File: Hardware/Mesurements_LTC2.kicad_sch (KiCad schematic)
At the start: 12 parts, among them Q2 NPN, U2 BQ79614PAPRQ1

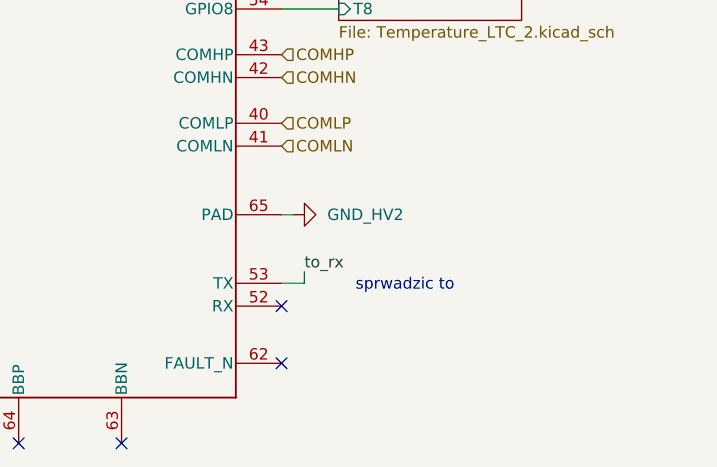
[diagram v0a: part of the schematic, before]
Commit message: Dodano diody TVS na każdej części zasilania, zmieniono bezpieczniki, podzielono bezpieczniki na bezpieczniki do prądów wewnętrznych oraz zewnętrznych,poprawiono małe błedy
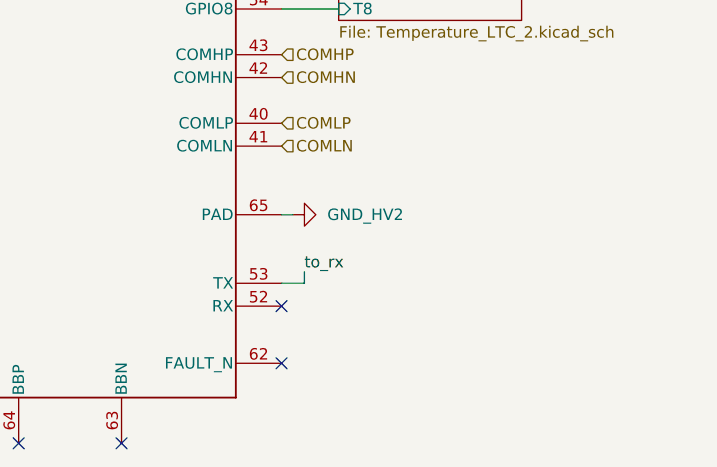
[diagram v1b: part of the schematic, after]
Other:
- note removed: "sprwadzic to"
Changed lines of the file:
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@@
 	(generator_version "9.0")
 	(paper "A4")
-	(text "sprwadzic to\n"
-		(exclude_from_sim no)
-		(at 150.876 131.064 0)
-		(effects
-			(font
-				(size 1.27 1.27)
-			)
-		)
-	)
 	(text "max 370ohm\n"
 		(exclude_from_sim no)

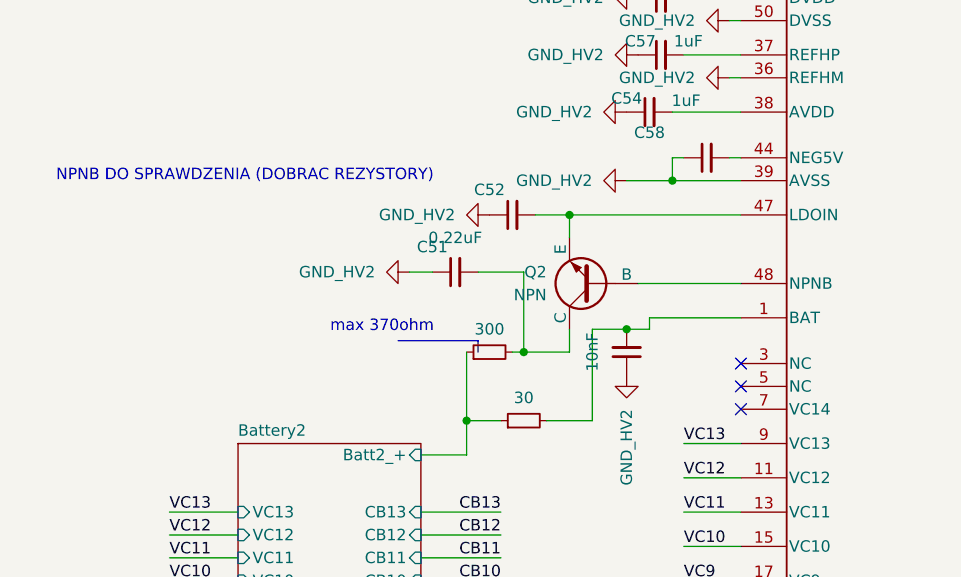
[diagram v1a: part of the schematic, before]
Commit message: dodano pozostale datasheety, zmieniono blad w usb
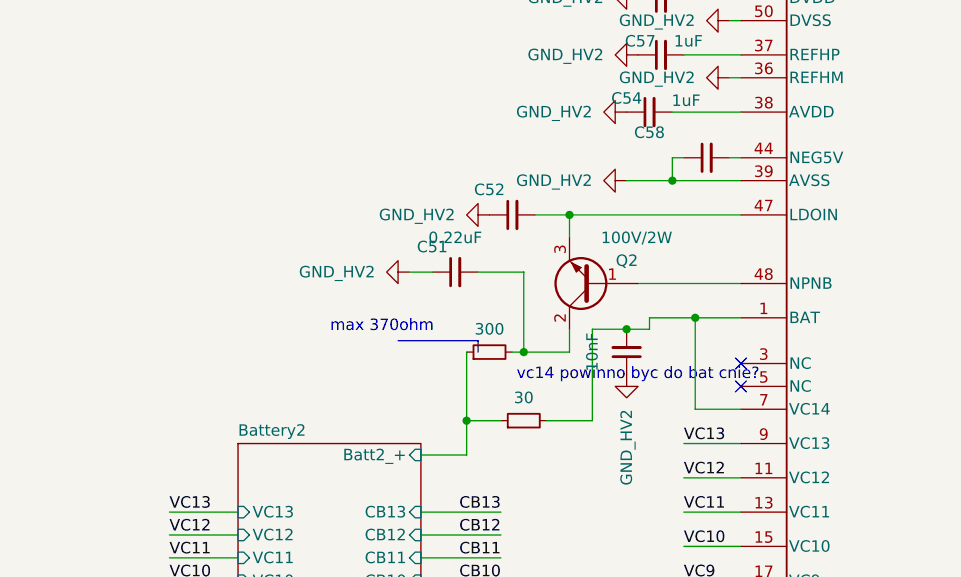
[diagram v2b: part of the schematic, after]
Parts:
- removed Q2: NPN, Package_TO_SOT_SMD:SOT-223-3_TabPin2, symbol Simulation_SPICE:NPN
- added Q2: 100V/2W, Package_TO_SOT_SMD:SOT-223-3_TabPin2, symbol Device:Q_NPN_BCE
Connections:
- net at C53.2, R66.2, U2.1 (BAT): now also U2.7 (VC14)
- net at C52.2, U2.47 (LDOIN): now also Q2.3 (E)
- net at U2.48 (NPNB): now also Q2.1 (B)
- net at C51.2, R64.2: now also Q2.2 (C)
- no-connect marks 10 -> 9
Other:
- note added: "vc14 powinno byc do bat cnie?"
- note removed: "NPNB DO SPRAWDZENIA (DOBRAC REZYSTORY)"
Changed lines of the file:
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@@
 	(generator_version "9.0")
 	(paper "A4")
-	(text "max 370ohm\n"
+	(text "vc14 powinno byc do bat cnie?\n"
 		(exclude_from_sim no)
-		(at 51.562 78.486 0)
+		(at 80.01 83.82 0)
 		(effects
 			(font
@@
 		)
 	)
-	(text "NPNB DO SPRAWDZENIA (DOBRAC REZYSTORY)\n"
+	(text "max 370ohm\n"
 		(exclude_from_sim no)
-		(at 36.322 61.722 0)
+		(at 51.562 78.486 0)
 		(effects
 			(font
@@
 	)
 	(junction
+		(at 86.36 77.47)
+		(diameter 0)
+		(color 0 0 0 0)
+	)
+	(junction
 		(at 60.96 88.9)
 		(diameter 0)
@@
 		(at 137.16 139.7)
 	)
-	(no_connect
-		(at 91.44 87.63)
-	)
 	(wire
 		(pts
@@
 	(wire
 		(pts
-			(xy 81.28 77.47) (xy 91.44 77.47)
+			(xy 81.28 77.47) (xy 86.36 77.47)
 		)
 		(stroke
@@
 	(wire
 		(pts
+			(xy 91.44 87.63) (xy 86.36 87.63)
+		)
+		(stroke
+			(width 0)
+			(type default)
+		)
+	)
+	(wire
+		(pts
 			(xy 67.31 72.39) (xy 62.23 72.39)
 		)
@@
 	(wire
 		(pts
+			(xy 86.36 87.63) (xy 86.36 77.47)
+		)
+		(stroke
+			(width 0)
+			(type default)
+		)
+	)
+	(wire
+		(pts
 			(xy 85.09 48.26) (xy 91.44 48.26)
 		)
@@
 	(wire
 		(pts
+			(xy 86.36 77.47) (xy 91.44 77.47)
+		)
+		(stroke
+			(width 0)
+			(type default)
+		)
+	)
+	(wire
+		(pts
 			(xy 74.93 88.9) (xy 74.93 78.74)
 		)
@@
 	)
 	(symbol
+		(lib_id "Device:Q_NPN_BCE")
+		(at 74.93 73.66 180)
+		(unit 1)
+		(exclude_from_sim no)
+		(in_bom yes)
+		(on_board yes)
+		(dnp no)
+		(property "Reference" "Q2"
+			(at 80.01 71.12 0)
+			(effects
+				(font
+					(size 1.27 1.27)
+				)
+				(justify left)
+			)
+		)
+		(property "Value" "100V/2W"
+			(at 83.82 68.58 0)
+			(effects
+				(font
+					(size 1.27 1.27)
+				)
+				(justify left)
+			)
+		)
+		(property "Footprint" "Package_TO_SOT_SMD:SOT-223-3_TabPin2"
+			(at 69.85 76.2 0)
+			(effects
+				(font
+					(size 1.27 1.27)
+				)
+				(hide yes)
+			)
+		)
+		(property "Datasheet" "https://eu.mouser.com/ProductDetail/Diodes-Incorporated/FZT653TA?qs=rI7uf1IzohQqmHMCtqURKQ%3D%3D"
+			(at 74.93 73.66 0)
+			(effects
+				(font
+					(size 1.27 1.27)
+				)
+				(hide yes)
+			)
+		)
+		(property "Description" "NPN transistor, base/collector/emitter"
+			(at 74.93 73.66 0)
+			(effects
+				(font
+					(size 1.27 1.27)
+				)
+				(hide yes)
+			)
+		)
+		(property "TME Electronic Components Part Number" ""
+			(at 74.93 73.66 0)
+			(effects
+				(font
+					(size 1.27 1.27)
+				)
+				(hide yes)
+			)
+		)
+		(property "TME Electronic Components Price/Stock" ""
+			(at 74.93 73.66 0)
+			(effects
+				(font
+					(size 1.27 1.27)
+				)
+				(hide yes)
+			)
+		)
+		(property "Arrow Part Number" ""
+			(at 74.93 73.66 0)
+			(effects
+				(font
+					(size 1.27 1.27)
+				)
+				(hide yes)
+			)
+		)
+		(property "Arrow Price/Stock" ""
+			(at 74.93 73.66 0)
+			(effects
+				(font
+					(size 1.27 1.27)
+				)
+				(hide yes)
+			)
+		)
+		(property "Mouser Part Number" "522-FZT653TA"
+			(at 74.93 73.66 0)
+			(effects
+				(font
+					(size 1.27 1.27)
+				)
+				(hide yes)
+			)
+		)
+		(pin "1"
+		)
+		(pin "3"
+		)
+		(pin "2"
+		)
+		(instances
+			(project "BMS"
+				(path "/26289bb6-56bc-4ca1-b1a2-18d58d1afdf5/99f7ea83-6836-44ea-889b-f0d453e84b38"
+					(reference "Q2")
+					(unit 1)
+				)
+			)
+		)
+	)
+	(symbol
 		(lib_id "BQ79612PAPRQ1:BQ79616PAPRQ1")
 		(at 114.3 87.63 0)
@@
 					(unit 1)
 				)
-			)
-		)
-	)
-	(symbol
-		(lib_id "Simulation_SPICE:NPN")
-		(at 74.93 73.66 180)
-		(unit 1)
-		(exclude_from_sim no)
-		(in_bom yes)
-		(on_board yes)
-		(dnp no)
-		(fields_autoplaced yes)
-		(property "Reference" "Q2"
-			(at 69.85 72.3899 0)
-			(effects
-				(font
-					(size 1.27 1.27)
-				)
-				(justify left)
-			)
-		)
-		(property "Value" "NPN"
-			(at 69.85 74.9299 0)
-			(effects
-				(font
-					(size 1.27 1.27)
-				)
-				(justify left)
-			)
-		)
-		(property "Footprint" "Package_TO_SOT_SMD:SOT-223-3_TabPin2"
-			(at 11.43 73.66 0)
-			(effects
-				(font
-					(size 1.27 1.27)
-				)
-				(hide yes)
-			)
-		)
-		(property "Datasheet" "https://eu.mouser.com/c/semiconductors/discrete-semiconductors/transistors/?collector-%20base%20voltage%20vcbo=100%20V&collector-%20emitter%20voltage%20vceo%20max=80%20V&mounting%20style=SMD%2FSMT&transistor%20polarity=NPN"
-			(at 11.43 73.66 0)
-			(effects
-				(font
-					(size 1.27 1.27)
-				)
-				(hide yes)
-			)
-		)
-		(property "Description" "NPN"
-			(at 74.93 73.66 0)
-			(effects
-				(font
-					(size 1.27 1.27)
-				)
-				(hide yes)
-			)
-		)
-		(property "opis" "NPN"
-			(at 74.93 73.66 0)
-			(effects
-				(font
-					(size 1.27 1.27)
-				)
-				(hide yes)
-			)
-		)
-		(property "Sim.Type" "GUMMELPOON"
-			(at 74.93 73.66 0)
-			(effects
-				(font
-					(size 1.27 1.27)
-				)
-				(hide yes)
-			)
-		)
-		(property "Sim.Pins" "1=C 2=B 3=E"
-			(at 74.93 73.66 0)
-			(effects
-				(font
-					(size 1.27 1.27)
-				)
-				(hide yes)
-			)
-		)
-		(pin "1"
-		)
-		(pin "2"
-		)
-		(pin "3"
-		)
-		(instances
-			(project "BMS"
-				(path "/26289bb6-56bc-4ca1-b1a2-18d58d1afdf5/99f7ea83-6836-44ea-889b-f0d453e84b38"
-					(reference "Q2")
-					(unit 1)
-				)

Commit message: Wersja V1.0 gotowa, wysłana do produckji
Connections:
- net to_rx: now also U2.52 (RX); no longer U2.53 (TX)
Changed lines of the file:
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@@
 	)
 	(no_connect
-		(at 137.16 133.35)
+		(at 137.16 130.81)
 	)
 	(no_connect
@@
 	(wire
 		(pts
-			(xy 139.7 130.81) (xy 137.16 130.81)
-		)
-		(stroke
-			(width 0)
-			(type default)
-		)
-	)
-	(wire
-		(pts
 			(xy 137.16 41.91) (xy 143.51 41.91)
 		)
@@
 	(wire
 		(pts
-			(xy 139.7 129.54) (xy 139.7 130.81)
-		)
-		(stroke
-			(width 0)
-			(type default)
-		)
-	)
-	(wire
-		(pts
 			(xy 55.88 121.92) (xy 64.77 121.92)
 		)
@@
 		(pts
 			(xy 85.09 137.16) (xy 91.44 137.16)
+		)
+		(stroke
+			(width 0)
+			(type default)
+		)
+	)
+	(wire
+		(pts
+			(xy 137.16 133.35) (xy 139.7 133.35)
 		)
 		(stroke
@@
 	)
 	(label "to_rx"
-		(at 139.7 129.54 0)
+		(at 139.7 133.35 0)
 		(effects
 			(font

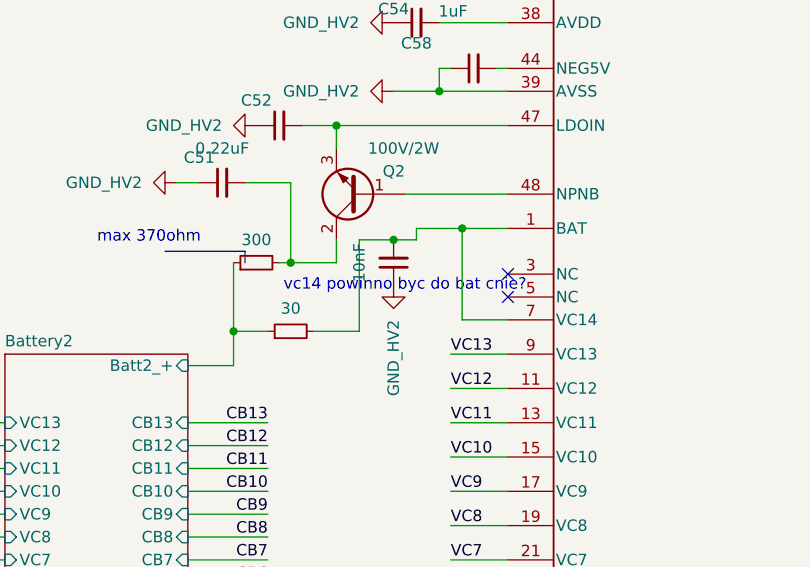
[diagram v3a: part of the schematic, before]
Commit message: Dodano podstawy komunikacji CAN , nie przeprowadzono jescze weryfikacji działania kodu
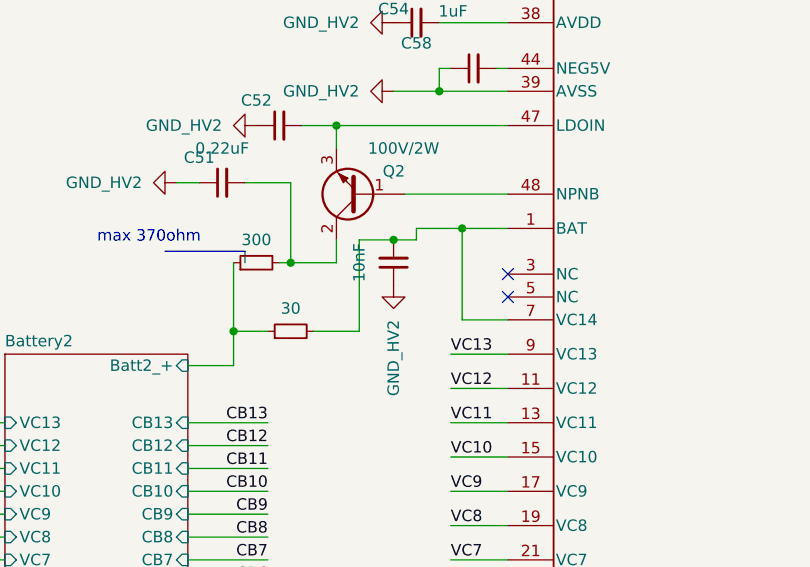
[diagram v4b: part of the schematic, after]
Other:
- note removed: "vc14 powinno byc do bat cnie?"
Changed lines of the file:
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@@
 	(generator_version "9.0")
 	(paper "A4")
-	(text "vc14 powinno byc do bat cnie?\n"
-		(exclude_from_sim no)
-		(at 80.01 83.82 0)
-		(effects
-			(font
-				(size 1.27 1.27)
-			)
-		)
-	)
 	(text "max 370ohm\n"
 		(exclude_from_sim no)
